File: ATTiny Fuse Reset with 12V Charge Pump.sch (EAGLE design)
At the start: 45 parts, among them U2 ARDUINOR3-BPLACE

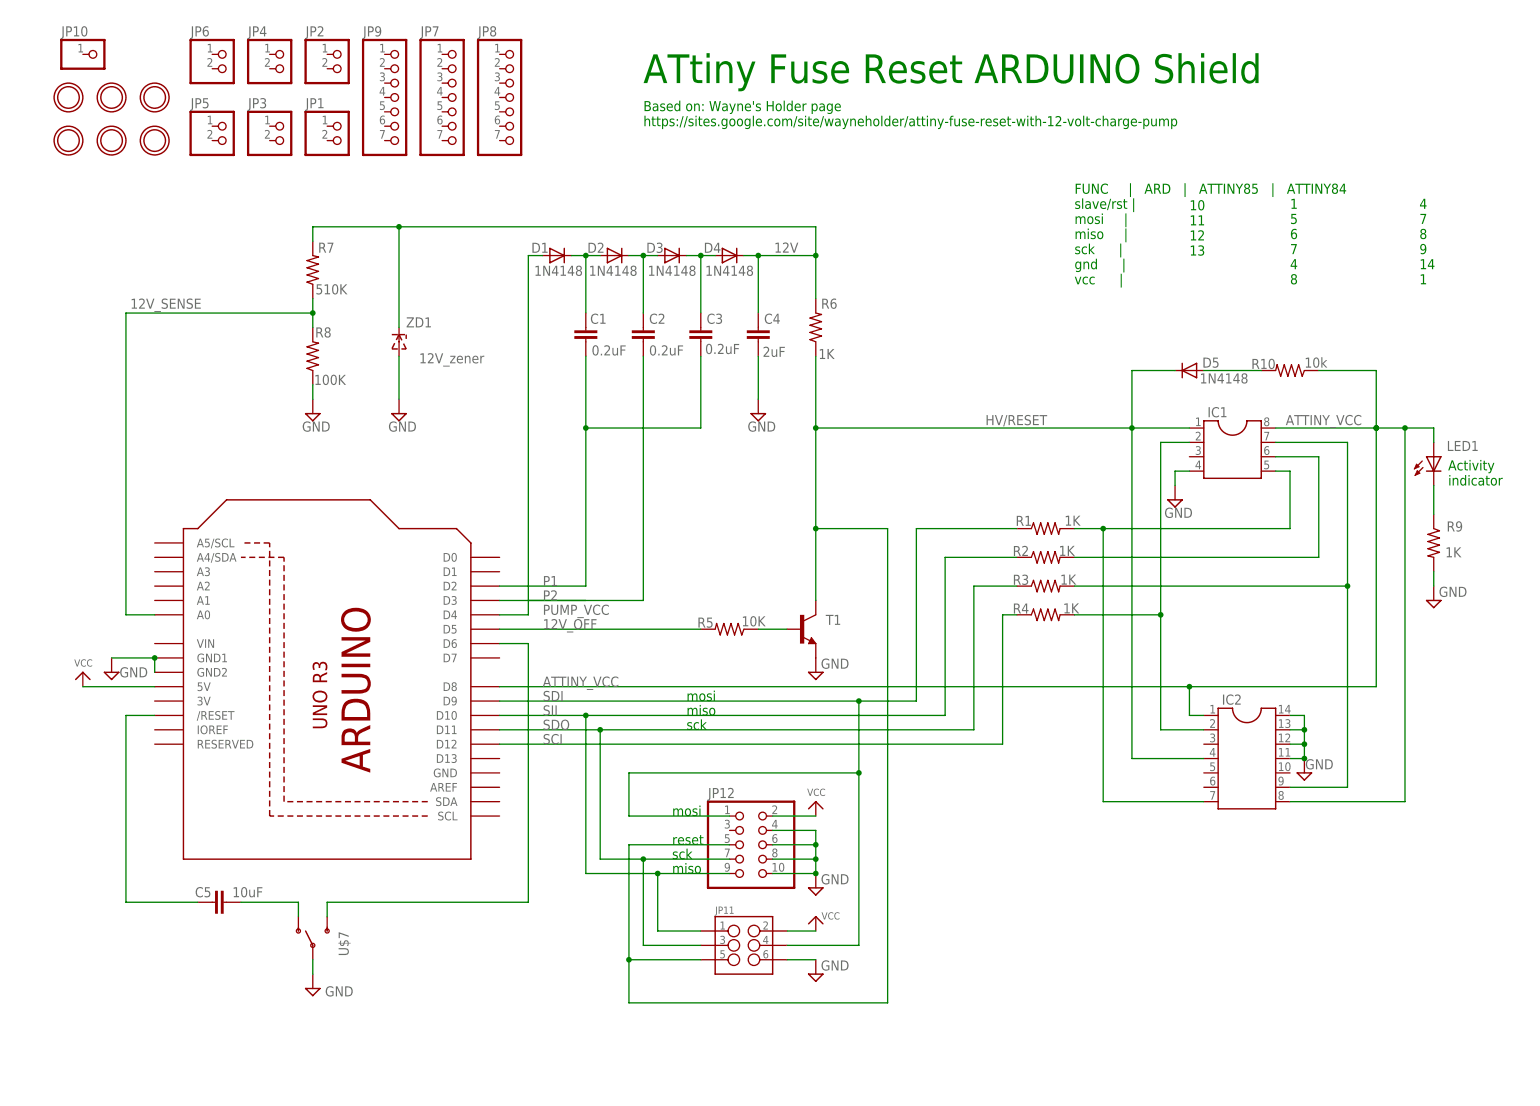
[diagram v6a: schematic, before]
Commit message: layout and package of attami added
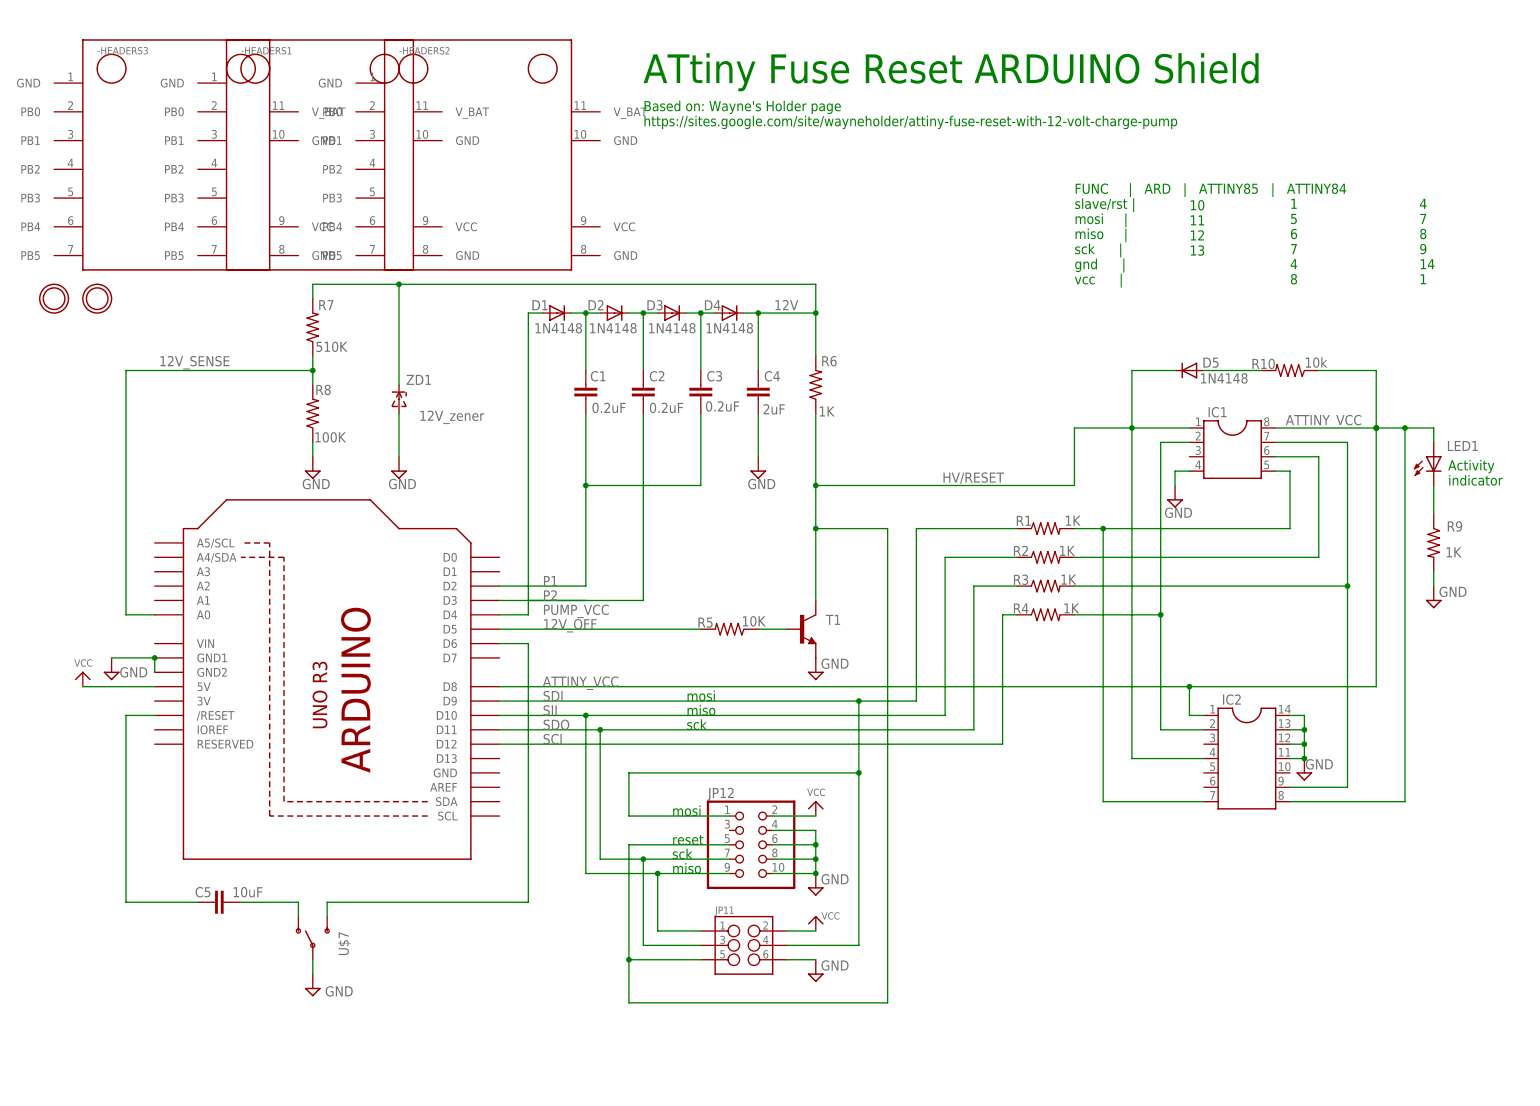
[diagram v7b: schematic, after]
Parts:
- removed JP1, JP2, JP3, JP4, JP5, JP6: (no value), ATtami:HEADER-1X2ROUND
- removed JP10: (no value), ATtami:PINHD-1X1
- removed JP7, JP8, JP9: (no value), ATtami:HEADER-1X7ROUND
- removed U$1, U$2, U$3, U$4: MOUNTINGHOLE2.0, ATtami:MOUNTINGHOLE2.0
- added -HEADERS1, -HEADERS2: (no value), ATtami:ATTANI_BREAKOUT_PINSNOHEAD
- added -HEADERS3: (no value), ATtami:ATTANI_BREAKOUT_PINS
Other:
- moved on the sheet: C1, C2, C3, C4, D1, D2, D3, D4, R6, R7, R8, ZD1
